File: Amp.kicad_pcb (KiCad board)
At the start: 2 copper layers, 29 parts, among them P1 100k, U1 ECC83, U2 EL34, U3 EL34

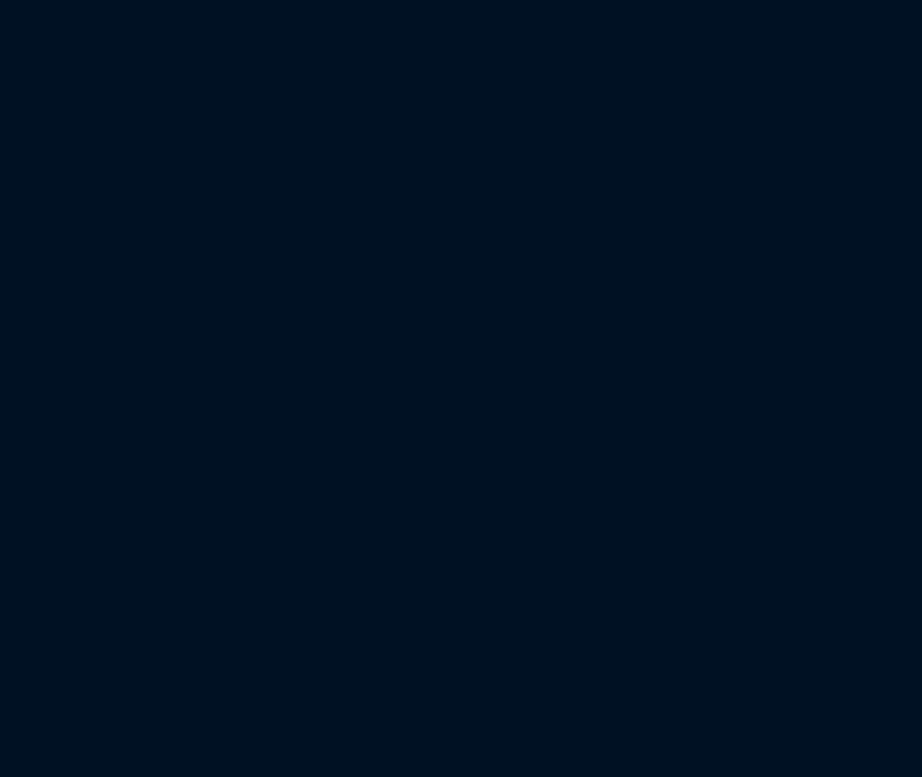
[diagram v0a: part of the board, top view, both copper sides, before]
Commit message: Adding footprints
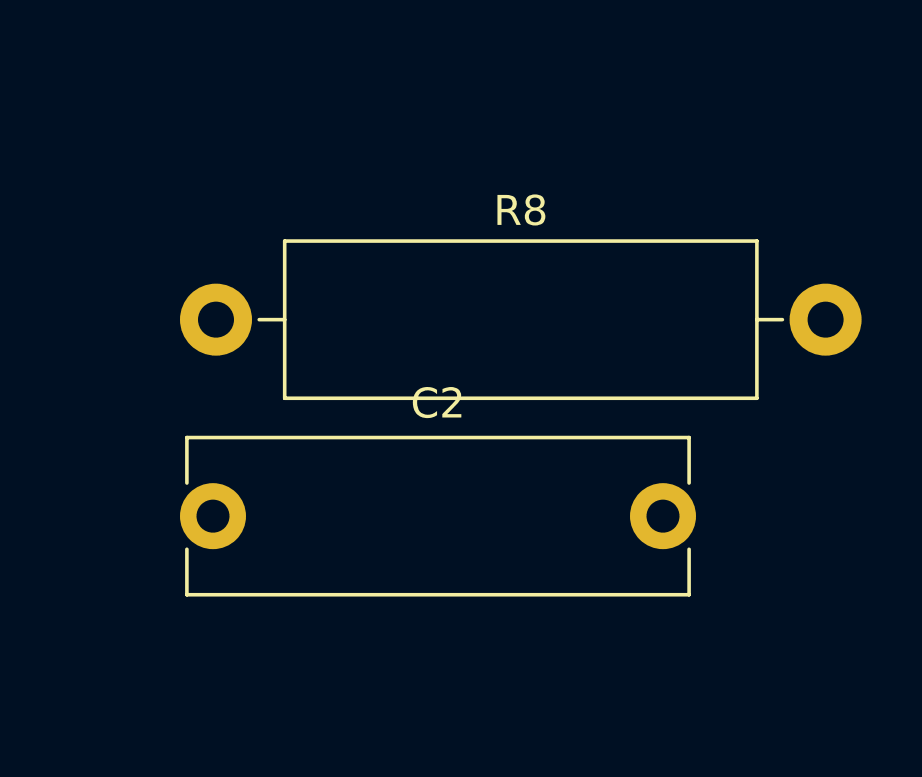
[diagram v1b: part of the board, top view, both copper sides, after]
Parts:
- added C2: 220n 400v, Capacitor_THT:C_Rect_L16.5mm_W5.0mm_P15.00mm_MKT, F.Cu at (228.6, 147.3)
- added R8: 10k 2W, Resistor_THT:R_Axial_DIN0516_L15.5mm_D5.0mm_P20.32mm_Horizontal, F.Cu at (228.7, 140.8)
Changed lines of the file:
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@@
+    )
+  )
+  (footprint "Capacitor_THT:C_Rect_L16.5mm_W5.0mm_P15.00mm_MKT" (layer "F.Cu")
+    (at 228.6 147.32)
+    (descr "C, Rect series, Radial, pin pitch=15.00mm, , length*width=16.5*5mm^2, Capacitor, https://en.tdk.eu/inf/20/20/db/fc_2009/MKT_B32560_564.pdf")
+    (tags "C Rect series Radial pin pitch 15.00mm  length 16.5mm width 5mm Capacitor")
+    (property "Sheetfile" "Amp.kicad_sch")
+    (property "Sheetname" "")
+    (attr through_hole)
+    (fp_text reference "C2" (at 7.5 -3.75) (layer "F.SilkS")
+      (effects (font (size 1 1) (thickness 0.15)))
+    )
+    (fp_text value "220n 400v" (at 7.5 3.75) (layer "F.Fab")
+      (effects (font (size 1 1) (thickness 0.15)))
+    )
+    (fp_text user "${REFERENCE}" (at 7.5 0) (layer "F.Fab")
+      (effects (font (size 1 1) (thickness 0.15)))
+    )
+    (fp_line (start -0.87 1.104) (end -0.87 2.62) (layer "F.SilkS") (width 0.12))
+    (fp_line (start -0.87 2.62) (end 15.87 2.62) (layer "F.SilkS") (width 0.12))
+    (fp_line (start -0.87 -2.62) (end -0.87 -1.104) (layer "F.SilkS") (width 0.12))
+    (fp_line (start -0.87 -2.62) (end 15.87 -2.62) (layer "F.SilkS") (width 0.12))
+    (fp_line (start 15.87 -2.62) (end 15.87 -1.104) (layer "F.SilkS") (width 0.12))
+    (fp_line (start 15.87 1.104) (end 15.87 2.62) (layer "F.SilkS") (width 0.12))
+    (fp_line (start 16.35 -2.75) (end -1.35 -2.75) (layer "F.CrtYd") (width 0.05))
+    (fp_line (start -1.35 -2.75) (end -1.35 2.75) (layer "F.CrtYd") (width 0.05))
+    (fp_line (start -1.35 2.75) (end 16.35 2.75) (layer "F.CrtYd") (width 0.05))
+    (fp_line (start 16.35 2.75) (end 16.35 -2.75) (layer "F.CrtYd") (width 0.05))
+    (fp_line (start -0.75 2.5) (end 15.75 2.5) (layer "F.Fab") (width 0.1))
+    (fp_line (start 15.75 2.5) (end 15.75 -2.5) (layer "F.Fab") (width 0.1))
+    (fp_line (start 15.75 -2.5) (end -0.75 -2.5) (layer "F.Fab") (width 0.1))
+    (fp_line (start -0.75 -2.5) (end -0.75 2.5) (layer "F.Fab") (width 0.1))
+    (pad "1" thru_hole circle locked (at 0 0) (size 2.2 2.2) (drill 1.1) (layers *.Cu *.Mask)
+      (net 24 "GND") (pintype "passive"))
+    (pad "2" thru_hole circle locked (at 15 0) (size 2.2 2.2) (drill 1.1) (layers *.Cu *.Mask)
+      (net 2 "Net-(C2-Pad2)") (pintype "passive"))
+    (model "${KICAD6_3DMODEL_DIR}/Capacitor_THT.3dshapes/C_Rect_L16.5mm_W5.0mm_P15.00mm_MKT.wrl"
+      (offset (xyz 0 0 0))
+      (scale (xyz 1 1 1))
+      (rotate (xyz 0 0 0))
     )
   )
@@
       (offset (xyz 0 0 0))
       (scale (xyz 1 1 1))
+      (rotate (xyz 0 0 0))
+    )
+  )
+  (footprint "Resistor_THT:R_Axial_DIN0516_L15.5mm_D5.0mm_P20.32mm_Horizontal" (layer "F.Cu")
+    (at 228.7 140.77)
+    (descr "Resistor, Axial_DIN0516 series, Axial, Horizontal, pin pitch=20.32mm, 2W, length*diameter=15.5*5mm^2, http://cdn-reichelt.de/documents/datenblatt/B400/1_4W%23YAG.pdf")
+    (tags "Resistor Axial_DIN0516 series Axial Horizontal pin pitch 20.32mm 2W length 15.5mm diameter 5mm")
+    (property "Sheetfile" "Amp.kicad_sch")
+    (property "Sheetname" "")
+    (attr through_hole)
+    (fp_text reference "R8" (at 10.16 -3.62) (layer "F.SilkS")
+      (effects (font (size 1 1) (thickness 0.15)))
+    )
+    (fp_text value "10k 2W" (at 10.16 3.62) (layer "F.Fab")
+      (effects (font (size 1 1) (thickness 0.15)))
+    )
+    (fp_text user "${REFERENCE}" (at 10.16 0) (layer "F.Fab")
+      (effects (font (size 1 1) (thickness 0.15)))
+    )
+    (fp_line (start 18.03 -2.62) (end 2.29 -2.62) (layer "F.SilkS") (width 0.12))
+    (fp_line (start 2.29 2.62) (end 18.03 2.62) (layer "F.SilkS") (width 0.12))
+    (fp_line (start 18.88 0) (end 18.03 0) (layer "F.SilkS") (width 0.12))
+    (fp_line (start 2.29 -2.62) (end 2.29 2.62) (layer "F.SilkS") (width 0.12))
+    (fp_line (start 18.03 2.62) (end 18.03 -2.62) (layer "F.SilkS") (width 0.12))
+    (fp_line (start 1.44 0) (end 2.29 0) (layer "F.SilkS") (width 0.12))
+    (fp_line (start 21.77 2.75) (end 21.77 -2.75) (layer "F.CrtYd") (width 0.05))
+    (fp_line (start -1.45 2.75) (end 21.77 2.75) (layer "F.CrtYd") (width 0.05))
+    (fp_line (start 21.77 -2.75) (end -1.45 -2.75) (layer "F.CrtYd") (width 0.05))
+    (fp_line (start -1.45 -2.75) (end -1.45 2.75) (layer "F.CrtYd") (width 0.05))
+    (fp_line (start 17.91 -2.5) (end 2.41 -2.5) (layer "F.Fab") (width 0.1))
+    (fp_line (start 2.41 -2.5) (end 2.41 2.5) (layer "F.Fab") (width 0.1))
+    (fp_line (start 20.32 0) (end 17.91 0) (layer "F.Fab") (width 0.1))
+    (fp_line (start 0 0) (end 2.41 0) (layer "F.Fab") (width 0.1))
+    (fp_line (start 17.91 2.5) (end 17.91 -2.5) (layer "F.Fab") (width 0.1))
+    (fp_line (start 2.41 2.5) (end 17.91 2.5) (layer "F.Fab") (width 0.1))
+    (pad "1" thru_hole circle locked (at 0 0) (size 2.4 2.4) (drill 1.2) (layers *.Cu *.Mask)
+      (net 23 "+A2") (pintype "passive"))
+    (pad "2" thru_hole oval locked (at 20.32 0) (size 2.4 2.4) (drill 1.2) (layers *.Cu *.Mask)
+      (net 26 "+A") (pintype "passive"))
+    (model "${KICAD6_3DMODEL_DIR}/Resistor_THT.3dshapes/R_Axial_DIN0516_L15.5mm_D5.0mm_P20.32mm_Horizontal.wrl"
+      (offset (xyz 0 0 0))
+      (scale (xyz 1 1 1))

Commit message: Update
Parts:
- added J1: Screw_Terminal_01x02, Connector:Banana_Jack_2Pin, F.Cu at (76.0, 190.5)
- added J2: AudioJack2, Connector_Audio:Jack_3.5mm_CUI_SJ-3523-SMT_Horizontal, F.Cu at (30.5, 101.6)
- added J3: Screw_Terminal_01x02, Connector:Banana_Jack_2Pin, F.Cu at (215.9, 73.7)
- added J4: Screw_Terminal_01x02, Connector:Banana_Jack_2Pin, F.Cu at (215.9, 91.4)
- added J5: Screw_Terminal_01x02, Connector:Banana_Jack_2Pin, F.Cu at (215.9, 106.7)
- moved P1 154.6 mm to (33.7, 91.4), turned to 90 degrees
- moved C1 143.1 mm to (55.9, 88.9), turned to 180 degrees
- moved C2 139.2 mm to (94.0, 111.8), turned to 180 degrees
- moved R14 133.7 mm to (172.7, 45.7), turned to 180 degrees
- moved R11 128.3 mm to (185.4, 50.8), turned to -90 degrees
- moved U1 123.2 mm to (88.9, 96.5)
- moved R2 123.1 mm to (43.2, 81.3)
- moved C9 122.5 mm to (108.5, 172.6), turned to 90 degrees
- moved R3 121.0 mm to (43.2, 96.5)
- moved R5 105.7 mm to (94.0, 73.7), turned to 180 degrees
- moved C5 105.6 mm to (109.2, 144.8), turned to 180 degrees
- moved R8 105.6 mm to (123.7, 152.4), turned to -90 degrees
- moved R1 95.4 mm to (63.5, 104.1), turned to 180 degrees
- moved R7 95.3 mm to (124.5, 88.9), turned to 180 degrees
- moved C6 92.0 mm to (195.6, 53.3), turned to -90 degrees
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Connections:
- D1 pad 4: unconnected-(D1-Pad4) -> Net-(D1-Pad4)
- P1 pad 1: unconnected-(P1-Pad1) -> Net-(P1-Pad1)
- R13 pad 1: unconnected-(R13-Pad1) -> Net-(R13-Pad1)
- R14 pad 1: unconnected-(R14-Pad1) -> Net-(R14-Pad1)
- U2 pad 3: unconnected-(U2-Pad3) -> Net-(U2-Pad3)
- U3 pad 3: unconnected-(U3-Pad3) -> Net-(U3-Pad3)

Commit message: Update
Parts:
- added ?: , , F.Cu at (27.9, 129.5)
- added ?: , , F.Cu at (111.8, 63.5)
- added ?: , , F.Cu at (208.3, 129.5)
- added F1: Fuse, Fuse:Fuseholder_Cylinder-5x20mm_Schurter_0031_8201_Horizontal_Open, F.Cu at (20.3, 190.5)
- added F2: Fuse, Fuse:Fuseholder_Cylinder-5x20mm_Schurter_0031_8201_Horizontal_Open, F.Cu at (83.8, 114.3)
- added F3: Fuse, Fuse:Fuseholder_Cylinder-5x20mm_Schurter_0031_8201_Horizontal_Open, F.Cu at (119.4, 114.3)
- added F4: Fuse, Fuse:Fuseholder_Cylinder-5x20mm_Schurter_0031_8201_Horizontal_Open, F.Cu at (149.9, 114.3)
- added J10: Conn_01x01_Female, Connector_Pin:Pin_D1.0mm_L10.0mm, F.Cu at (94.0, 63.5)
- added J11: Conn_01x01_Female, Connector_Pin:Pin_D1.0mm_L10.0mm, F.Cu at (129.5, 127.0)
- added J12: Conn_01x01_Female, Connector_Pin:Pin_D1.0mm_L10.0mm, F.Cu at (58.4, 63.5)
- added J13: Conn_01x01_Female, Connector_Pin:Pin_D1.0mm_L10.0mm, F.Cu at (170.2, 83.8)
- added J14: Conn_01x01_Female, Connector_Pin:Pin_D1.0mm_L10.0mm, F.Cu at (213.4, 81.3)
- added J6: Conn_01x01_Female, Connector_Pin:Pin_D1.0mm_L10.0mm, F.Cu at (142.2, 165.1)
- added J7: Conn_01x01, Connector_Pin:Pin_D1.0mm_L10.0mm, F.Cu at (137.2, 127.0)
- added J7: Conn_01x01_Female, Connector_Pin:Pin_D1.0mm_L10.0mm, F.Cu at (129.5, 134.6)
- added J8: Conn_01x01_Female, Connector_Pin:Pin_D1.0mm_L10.0mm, F.Cu at (205.7, 88.9)
- added J9: Conn_01x01, Connector_Pin:Pin_D1.0mm_L10.0mm, F.Cu at (137.2, 134.6)
- added J9: Conn_01x01_Female, Connector_Pin:Pin_D1.0mm_L10.0mm, F.Cu at (177.8, 66.0)
- added REF**: Banana_Jack_1Pin, Connector:Banana_Jack_1Pin, F.Cu at (27.9, 63.5)
- J1, J3, J4, J5: value Screw_Terminal_01x02 -> Conn_01x01_Female; footprint Connector:Banana_Jack_2Pin -> Connector_Pin:Pin_D1.0mm_L10.0mm
- moved J3 212.8 mm to (20.3, 157.5), turned to 0 degrees
- moved J4 157.1 mm to (94.0, 190.5), turned to 0 degrees
- moved J1 138.7 mm to (137.2, 66.0), turned to 0 degrees
- moved U3 70.4 mm to (200.7, 66.0), turned to 90 degrees
- moved R11 55.5 mm to (170.2, 104.1), turned to 180 degrees
- moved C6 51.4 mm to (177.8, 101.6), turned to 0 degrees
- moved R14 50.9 mm to (170.2, 96.5)
- moved C7 47.7 mm to (215.9, 88.9), turned to -90 degrees
- moved J5 41.9 mm to (175.3, 96.5), turned to 0 degrees
- moved R5 41.3 mm to (134.6, 81.3)
- moved R13 35.7 mm to (208.3, 96.5)
- moved R2 21.7 mm to (63.5, 88.9)
- moved U1 21.7 mm to (81.3, 76.2)
- moved C3 20.3 mm to (94.0, 81.3), turned to 0 degrees
- moved C4 20.2 mm to (94.0, 104.1), turned to 0 degrees
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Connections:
- J1 pad 1: Net-(D1-Pad4) -> Net-(U2-Pad3)
- J3 pad 1: Net-(U2-Pad3) -> Net-(F1-Pad2)
- J4 pad 1: +A -> Net-(D1-Pad4)
- J5 pad 1: Net-(R13-Pad1) -> Net-(R14-Pad1)
- U1 pad 4: unconnected-(U1-Pad4) -> Net-(U1-Pad4)
- U1 pad 5: unconnected-(U1-Pad5) -> Net-(U1-Pad5)
- U1 pad 9: unconnected-(U1-Pad9) -> Net-(U1-Pad9)
- U2 pad 2: unconnected-(U2-Pad2) -> Net-(U2-Pad2)
- U2 pad 7: unconnected-(U2-Pad7) -> Net-(U2-Pad7)
- U3 pad 2: unconnected-(U3-Pad2) -> Net-(U3-Pad2)
- U3 pad 7: unconnected-(U3-Pad7) -> Net-(U3-Pad7)
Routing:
- net GND: track 0.00 -> 592.6 mm
- net Net-(U3-Pad2): track 0.00 -> 159.9 mm
- net +A: track 0.00 -> 131.9 mm
- net +A2: track 0.00 -> 114.4 mm
- net Net-(U2-Pad2): track 0.00 -> 84.9 mm
- net Net-(R15-Pad1): track 0.00 -> 83.3 mm
- net Net-(C3-Pad2): track 0.00 -> 71.4 mm
- net Net-(C4-Pad2): track 0.00 -> 68.8 mm
- net Net-(C7-Pad1): track 0.00 -> 66.2 mm
- net Net-(C6-Pad1): track 0.00 -> 65.8 mm
- net Net-(D1-Pad3): track 0.00 -> 58.7 mm
- net Net-(R10-Pad1): track 0.00 -> 57.1 mm
- net Net-(F2-Pad2): track 0.00 -> 49.9 mm
- net Net-(U1-Pad9): track 0.00 -> 43.9 mm
- net Net-(C2-Pad2): track 0.00 -> 41.6 mm
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
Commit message: Update, cleanup
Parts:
- removed the J7 at (137.2, 127.0)
- removed the J9 at (137.2, 134.6)
- added J15: Conn_01x01_Female, Connector_Pin:Pin_D1.0mm_L10.0mm, F.Cu at (129.5, 134.6)
- added J16: Conn_01x01_Female, Connector_Pin:Pin_D1.0mm_L10.0mm, F.Cu at (137.2, 134.6)
- added J17: Conn_01x01_Female, Connector_Pin:Pin_D1.0mm_L10.0mm, F.Cu at (20.3, 144.8)
- moved J7 10.8 mm to (137.2, 127.0)
- moved R14 5.68 mm to (167.6, 91.4)
- moved J5 5.68 mm to (172.7, 91.4)
- moved R13 2.54 mm to (208.3, 94.0)
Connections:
- F3 pad 2: unconnected-(F3-Pad2) -> Net-(F3-Pad2)
- F4 pad 2: unconnected-(F4-Pad2) -> Net-(F4-Pad2)
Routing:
- net Net-(F3-Pad1): track 22.0 -> 0.00 mm
- net Net-(F4-Pad2): track 0.00 -> 13.8 mm
- net Net-(F4-Pad1): track 13.8 -> 0.00 mm
- net Net-(F3-Pad2): track 0.00 -> 11.1 mm
- net Net-(C6-Pad1): track 65.8 -> 57.3 mm
- net Net-(R14-Pad2): track 33.6 -> 25.4 mm
- net GND: track 592.6 -> 599.8 mm
- net Net-(R13-Pad2): track 28.6 -> 25.0 mm
- net Net-(R10-Pad1): track 57.1 -> 60.1 mm
- net Net-(R13-Pad1): track 8.67 -> 6.13 mm
- net Net-(U1-Pad4): track 19.9 -> 17.8 mm
- net Net-(U1-Pad5): track 14.8 -> 12.7 mm
- added copper zone on B.Cu, net Earth
- added copper zone on F.Cu, net Earth

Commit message: Cosmetic/cleanup
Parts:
- moved C9 36.9 mm to (117.4, 148.5)
- moved F1 36.9 mm to (21.6, 153.7)
- moved J4 36.9 mm to (95.2, 153.7)
- moved C1 36.9 mm to (57.1, 52.1)
- moved C7 36.9 mm to (217.2, 52.1)
- moved J1 36.9 mm to (138.4, 29.2)
- moved J8 36.9 mm to (207.0, 52.1)
- moved J9 36.9 mm to (179.1, 29.2)
- moved P1 36.9 mm to (34.9, 54.6)
- moved R13 36.9 mm to (209.6, 57.1)
- moved R2 36.9 mm to (64.8, 52.1)
- moved R7 36.9 mm to (110.5, 52.1)
- moved R9 36.9 mm to (135.9, 52.1)
- moved U1 36.9 mm to (82.5, 39.4)
- moved U2 36.9 mm to (163.8, 29.2)
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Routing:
- net Net-(C6-Pad1): track 57.3 -> 53.5 mm
- net GND: track 599.8 -> 600.8 mm
- added copper zone on B.Cu, net GND
- added copper zone on F.Cu, net GND
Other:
- board outline added: 218.4 x 147.3 mm

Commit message: Update
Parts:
- renumbered REF** to REF
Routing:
- net GND: track 600.8 -> 475.3 mm, vias 0 -> 33
- net +A2: track 114.4 -> 115.1 mm, vias 0 -> 3
